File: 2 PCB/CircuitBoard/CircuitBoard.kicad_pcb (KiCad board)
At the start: 2 copper layers, 49 parts, among them J1 Conn_01x04_Male, J10 Conn_01x04_Male, J11 Conn_01x04_Male, J12 Conn_01x04_Male, J13 Conn_01x04_Male, J14 Conn_01x04_Male, J15 Conn_01x04_Male, J16 Conn_01x04_Male, J17 Conn_01x04_Male, J18 Conn_01x04_Male, J19 Conn_01x04_Male, J2 Conn_01x04_Male, J20 Conn_01x04_Male, J21 Conn_01x24_Female, J22 Conn_01x24_Female, J23 Conn_01x04_Male, J24 Conn_01x04_Male, J25 Conn_01x04_Male, J26 Conn_01x04_Male, J27 Conn_01x04_Male, J28 Conn_01x04_Male, J29 Conn_01x04_Male, J3 Conn_01x04_Male, J30 Conn_01x04_Male, J31 Conn_01x04_Male, J32 Conn_01x04_Male, J33 Conn_01x04_Male, J34 Conn_01x04_Male, J35 Conn_01x04_Male, J36 Conn_01x04_Male, J37 Conn_01x04_Male, J38 Conn_01x04_Male, J39 Conn_01x04_Male, J4 Conn_01x04_Male, J40 Conn_01x04_Male, J41 Conn_01x04_Male, J42 Conn_01x04_Male, J5 Conn_01x04_Male, J6 Conn_01x04_Male, J7 Conn_01x04_Male, J8 Conn_01x04_Male, J9 Conn_01x04_Male, U1 TXS0108EPWR, U2 TXS0108EPWR, U3 TXS0108EPWR, U4 TXS0108EPWR, U5 TXS0108EPWR

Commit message: Added Parallel LEDs Commands and worked on Circuit Board
Parallel LED Commands allow for sigificantly faster data sending to LEDs and Circuit board is mostly finalized and was reviewed and confirmed to be good.
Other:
- board outline added: 79.8 x 138.9 mm

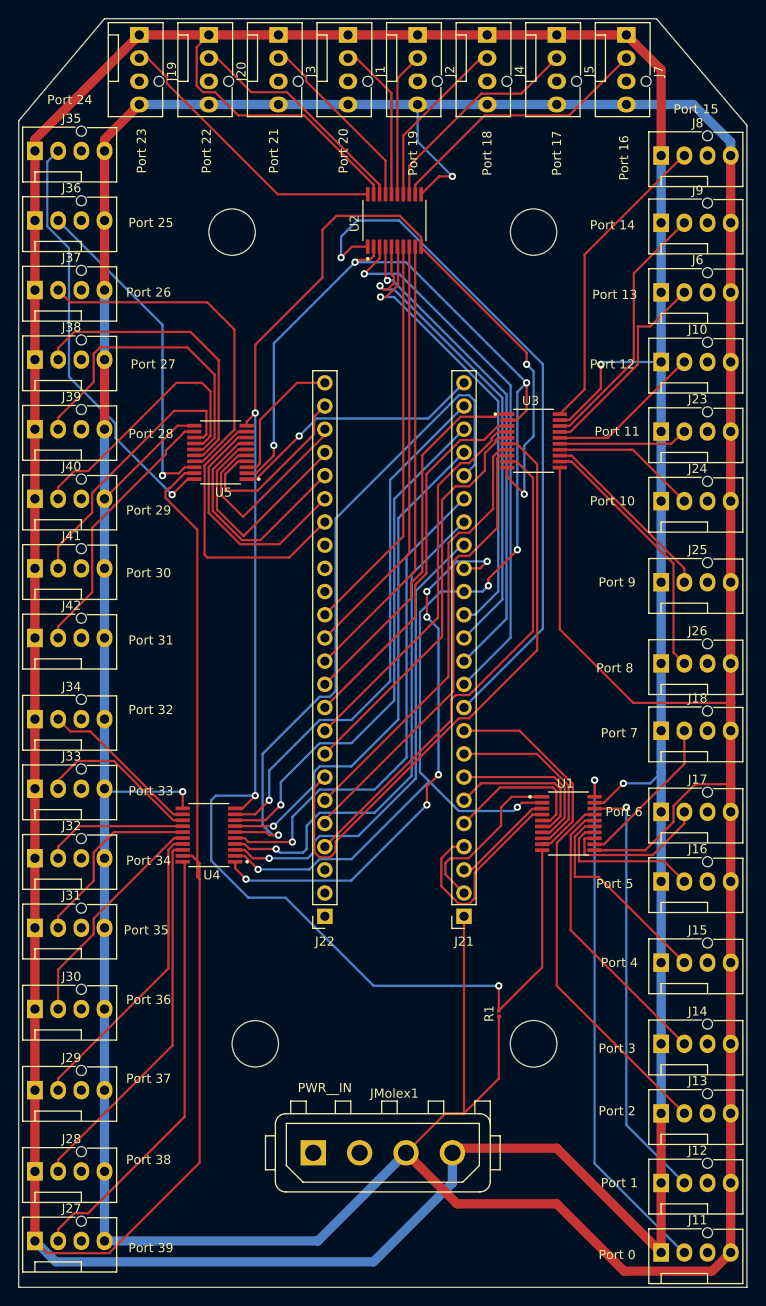
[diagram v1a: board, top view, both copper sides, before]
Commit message: Production PCB Added
Production PCB Added it was noticed since prodution there is an issue with the PCB that needs to be addressed in a future update. For now it can be fixed mostly by ripping the resistor off the board. Ideally then a wire will be soldered in its place to 3.3V
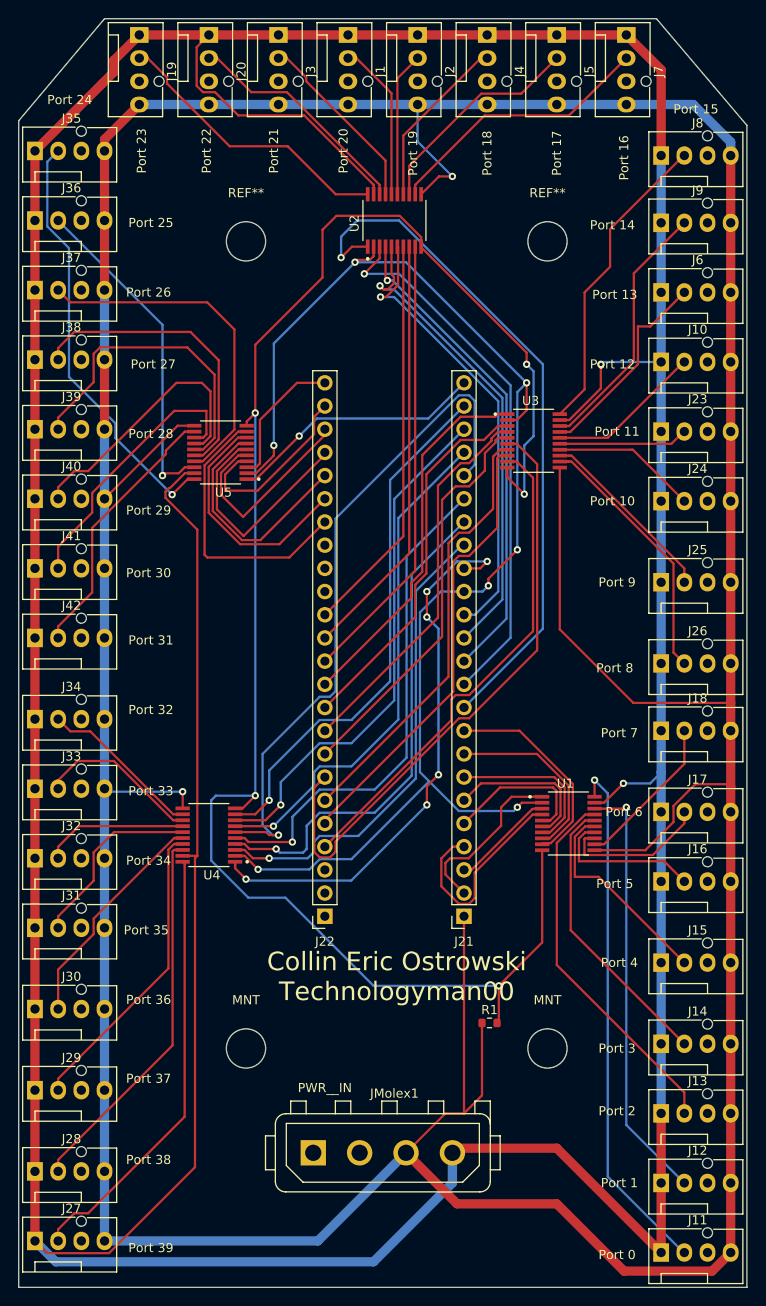
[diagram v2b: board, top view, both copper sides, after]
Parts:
- added MNT: MountingHole_4.3mm_M4, MountingHole:MountingHole_4.3mm_M4, F.Cu at (143.8, 158.0)
- added MNT: MountingHole_4.3mm_M4, MountingHole:MountingHole_4.3mm_M4, F.Cu at (110.7, 158.0)
- added REF**: MountingHole_4.3mm_M4, MountingHole:MountingHole_4.3mm_M4, F.Cu at (143.8, 69.6)
- added REF**: MountingHole_4.3mm_M4, MountingHole:MountingHole_4.3mm_M4, F.Cu at (110.7, 69.6)
- R1: footprint Resistor_SMD:R_0201_0603Metric -> Resistor_SMD:R_0603_1608Metric
- moved R1 1.44 mm to (137.4, 155.2), turned to 0 degrees
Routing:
- net Net-(J1-Pad1): track 567.2 -> 564.6 mm
- net Net-(J1-Pad4): track 531.2 -> 529.5 mm
- net Net-(R1-Pad2): track 190.4 -> 189.1 mm
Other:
- outline, holes or cut-outs redrawn
- board text added: "Collin Eric Ostrowski Technologyman00"

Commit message: PCB V2 & Case Work & Code Updates
PCB Version 2 started and completed. This makes it smaller and should fix the issues with having to solder a patch wire to the board. It also makes pin 13 no longer used for controlling the connected RGB components as it should not glow constantly which could disrupt RGB patterns. The new PCB also uses a much better mounting system for the Molex power connector. It also increased the trace width for the power traces to increase the current capabilities. As well a new case was started for covering the PCB inside a computer. Lastly, the Default pattern was bug fixed to no longer have issues with the MAXPIXELS constant being under 255. It also reflects the PCB change for pin 13.
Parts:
- removed R1: 10k, Resistor_SMD:R_0603_1608Metric
- JMolex1: footprint Connector_TE-Connectivity:TE_MATE-N-LOK_350211-1_1x04_P5.08mm_Vertical -> Molex:7708461
- moved JMolex1 10.5 mm to (126.5, 175.8), turned to 180 degrees
- renumbered REF** to MNT
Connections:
- U1 pad 10: Net-(R1-Pad2) -> Net-(J21-Pad15)
- U2 pad 10: Net-(R1-Pad2) -> Net-(J21-Pad15)
- U3 pad 10: Net-(R1-Pad2) -> Net-(J21-Pad15)
- U4 pad 10: Net-(R1-Pad2) -> Net-(J21-Pad15)
- U5 pad 10: Net-(R1-Pad2) -> Net-(J21-Pad15)
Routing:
- net Net-(R1-Pad2): track 189.1 -> 0.00 mm, vias 5 -> 0
- net Net-(J21-Pad15): track 153.7 -> 189.6 mm, vias 7 -> 10
- net Net-(J1-Pad4): track 529.5 -> 517.4 mm
- net Net-(J1-Pad1): track 564.6 -> 563.7 mm
